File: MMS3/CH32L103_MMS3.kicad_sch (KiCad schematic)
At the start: 2 parts

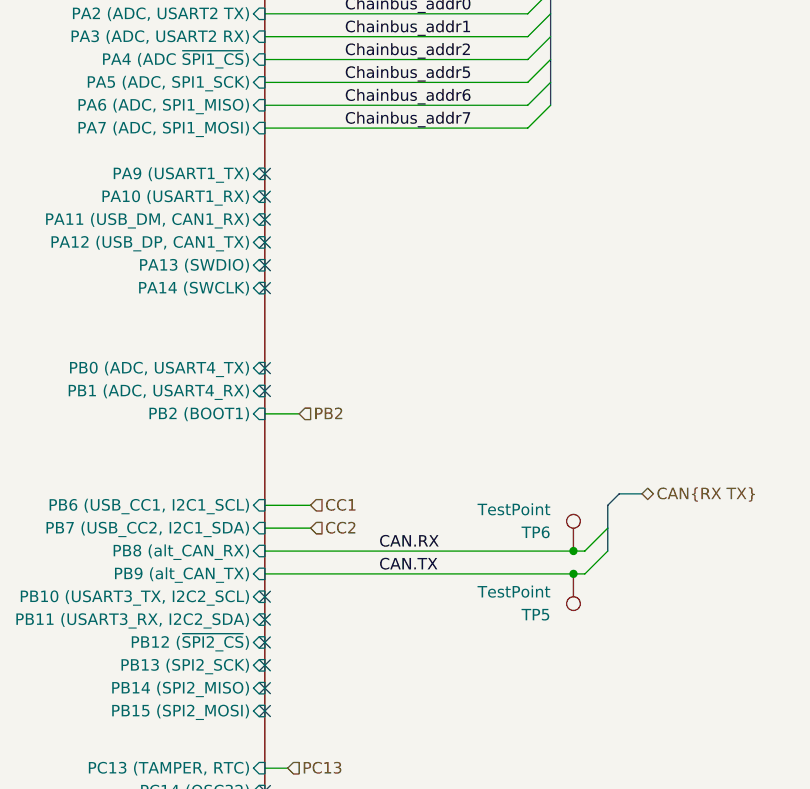
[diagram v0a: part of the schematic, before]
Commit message: updated schematic, removed annotation
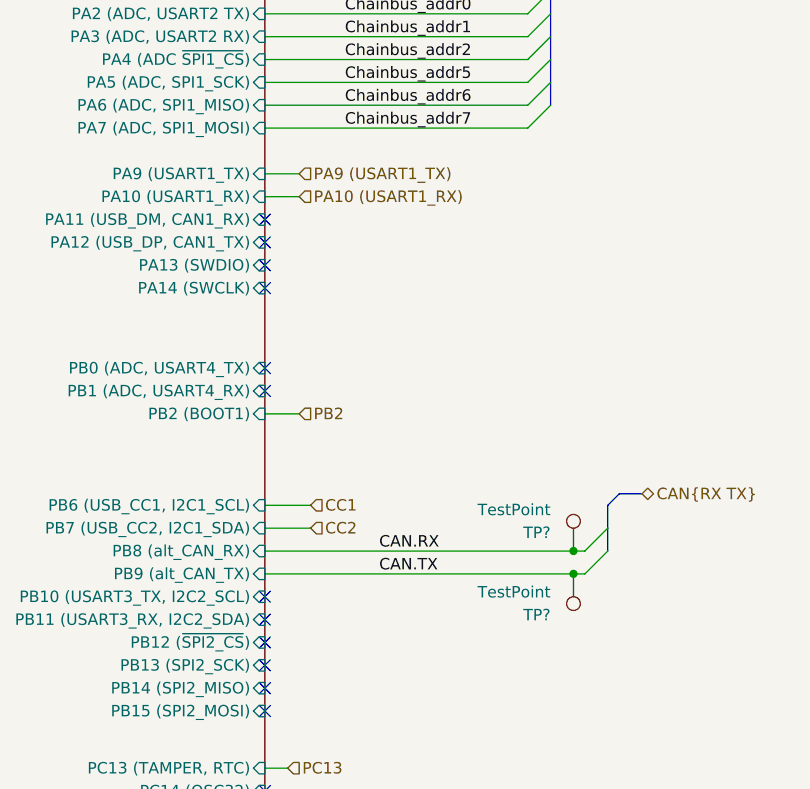
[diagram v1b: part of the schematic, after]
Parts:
- renumbered TP5 to TP?, TP6 to TP?
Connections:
- no-connect marks 21 -> 19
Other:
- title: MMS3 -> MMS3 CH32L103 Version
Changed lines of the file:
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@@
 	(paper "A4")
 	(title_block
-		(title "MMS3")
+		(title "MMS3 CH32L103 Version")
+		(date "2026-05-18")
 		(rev "XA1")
 		(company "(c) Modular Mechanica")
-		(comment 1 "Artem Horiunov")
-		(comment 2 "DESIGNED IN POLAND")
+		(comment 1 "DESIGNED IN POLAND")
+		(comment 2 "Forked by: Wojciech Szafranski")
+		(comment 3 "Made by: Artem Horiunov")
 	)
 	(junction
@@
 	)
 	(no_connect
-		(at 179.07 77.47)
-	)
-	(no_connect
 		(at 179.07 134.62)
 	)
@@
 	(no_connect
 		(at 179.07 143.51)
-	)
-	(no_connect
-		(at 179.07 74.93)
 	)
 	(no_connect
@@
 		)
 	)
+	(wire
+		(pts
+			(xy 179.07 74.93) (xy 182.88 74.93)
+		)
+		(stroke
+			(width 0)
+			(type default)
+		)
+	)
 	(bus
 		(pts
@@
 		(pts
 			(xy 179.07 59.69) (xy 208.28 59.69)
+		)
+		(stroke
+			(width 0)
+			(type default)
+		)
+	)
+	(wire
+		(pts
+			(xy 179.07 77.47) (xy 182.88 77.47)
 		)
 		(stroke
@@
 		)
 	)
+	(hierarchical_label "PA10 (USART1_RX)"
+		(shape input)
+		(at 182.88 77.47 0)
+		(effects
+			(font
+				(size 1.27 1.27)
+			)
+			(justify left)
+		)
+	)
 	(hierarchical_label "Chainbus_addr[0..7]"
 		(shape input)
@@
 		(shape input)
 		(at 184.15 111.76 0)
+		(effects
+			(font
+				(size 1.27 1.27)
+			)
+			(justify left)
+		)
+	)
+	(hierarchical_label "PA9 (USART1_TX)"
+		(shape input)
+		(at 182.88 74.93 0)
 		(effects
 			(font
@@
 		(dnp no)
 		(fields_autoplaced yes)
-		(property "Reference" "TP5"
+		(property "Reference" "TP?"
 			(at 210.82 123.9521 0)
 			(show_name no)
@@
 			(project "MMS3"
 				(path "/712cea22-140d-4c92-923f-f4998caf3ecd/ec639d08-3c03-4054-a7c4-c3d480e6d770"
-					(reference "TP5")
+					(reference "TP?")
 					(unit 1)
 				)
@@
 		(dnp no)
 		(fields_autoplaced yes)
-		(property "Reference" "TP6"
+		(property "Reference" "TP?"
 			(at 210.82 114.8081 0)
 			(show_name no)
@@
 			(project "MMS3"
 				(path "/712cea22-140d-4c92-923f-f4998caf3ecd/ec639d08-3c03-4054-a7c4-c3d480e6d770"
-					(reference "TP6")
+					(reference "TP?")
 					(unit 1)
 				)

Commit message: initial PCB update
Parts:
- gave numbers to parts that had none: 2
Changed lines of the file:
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@@
 		(dnp no)
 		(fields_autoplaced yes)
-		(property "Reference" "TP?"
+		(property "Reference" "TP3"
 			(at 210.82 123.9521 0)
 			(show_name no)
@@
 			(project "MMS3"
 				(path "/712cea22-140d-4c92-923f-f4998caf3ecd/ec639d08-3c03-4054-a7c4-c3d480e6d770"
-					(reference "TP?")
+					(reference "TP3")
 					(unit 1)
 				)
@@
 		(dnp no)
 		(fields_autoplaced yes)
-		(property "Reference" "TP?"
+		(property "Reference" "TP1"
 			(at 210.82 114.8081 0)
 			(show_name no)
@@
 			(project "MMS3"
 				(path "/712cea22-140d-4c92-923f-f4998caf3ecd/ec639d08-3c03-4054-a7c4-c3d480e6d770"
-					(reference "TP?")
+					(reference "TP1")
 					(unit 1)
 				)

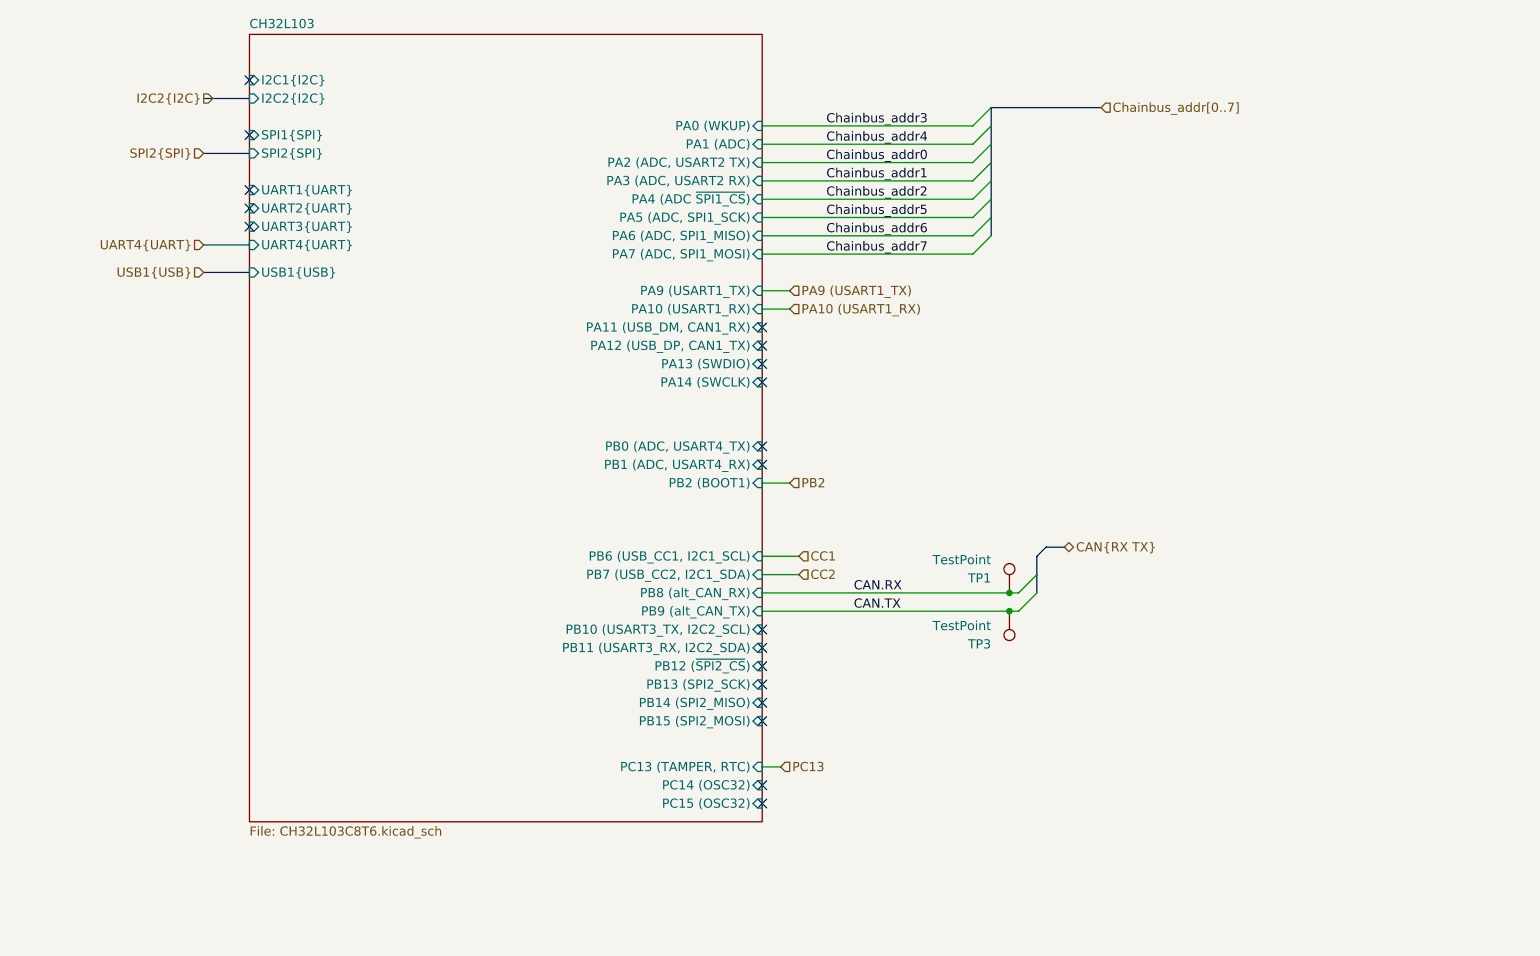
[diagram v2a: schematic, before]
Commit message: re-added onboard programmer
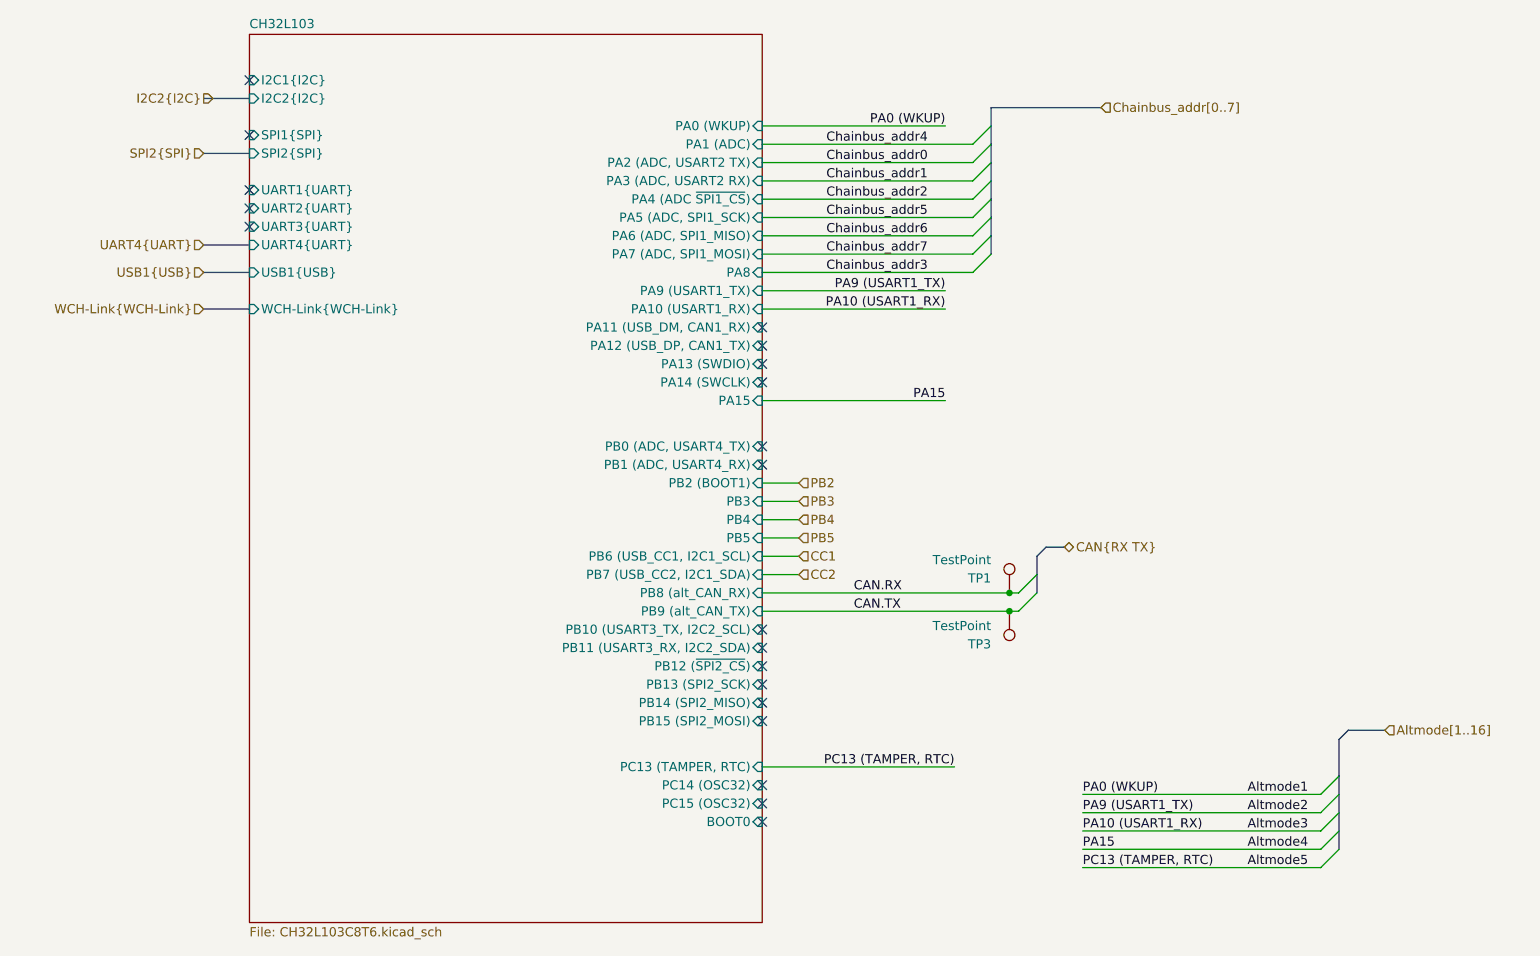
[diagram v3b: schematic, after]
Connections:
- no-connect marks 19 -> 20
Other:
- sheet CH32L103 ports: added BOOT0, PA15, PA8, PB3, PB4, PB5, WCH-Link{WCH-Link}; removed none
